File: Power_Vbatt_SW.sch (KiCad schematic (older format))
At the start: 14 parts, among them P5 XT60, Q1 IPD90P03P4L, Q2 BC817-40SMD, Q31 IPD90P03P4L

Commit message: Add more connector for thruster channels
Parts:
- added P2, P3, P4: XT60, Zeabus:XT60, symbol XT60
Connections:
- wire segments 30 -> 36
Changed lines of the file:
@@
 AR Path="/5625A3C6/56273268" Ref="Q18"  Part="1"
 AR Path="/5625A3D6/56273268" Ref="Q20"  Part="1"
-AR Path="/56273268" Ref="Q2"  Part="1"
-F 0 "Q2" H 5800 3775 50  0000 L CNN
+AR Path="/56273268" Ref="Q3"  Part="1"
+F 0 "Q3" H 5800 3775 50  0000 L CNN
 F 1 "BC817-40SMD" H 5800 3700 50  0000 L CNN
 F 2 "TO_SOT_Packages_SMD:SOT-23" H 5800 3625 50  0000 L CIN
@@
 AR Path="/5625A3C6/5627326B" Ref="#PWR048"  Part="1"
 AR Path="/5625A3D6/5627326B" Ref="#PWR051"  Part="1"
-AR Path="/5627326B" Ref="#PWR01"  Part="1"
-F 0 "#PWR01" H 5700 3700 50  0001 C CNN
+AR Path="/5627326B" Ref="#PWR1"  Part="1"
+F 0 "#PWR1" H 5700 3700 50  0001 C CNN
 F 1 "GND" H 5700 3800 50  0000 C CNN
 F 2 "" H 5700 3950 60  0000 C CNN
@@
 AR Path="/5625A3C6/5624F5C0" Ref="R45"  Part="1"
 AR Path="/5625A3D6/5624F5C0" Ref="R50"  Part="1"
-AR Path="/5624F5C0" Ref="R5"  Part="1"
-F 0 "R5" V 7380 4400 50  0000 C CNN
+AR Path="/5624F5C0" Ref="R6"  Part="1"
+F 0 "R6" V 7380 4400 50  0000 C CNN
 F 1 "1.2k" V 7300 4400 50  0000 C CNN
 F 2 "Resistors_SMD:R_0603" V 7230 4400 30  0001 C CNN
@@
 AR Path="/5625A3C6/5624F69A" Ref="R42"  Part="1"
 AR Path="/5625A3D6/5624F69A" Ref="R47"  Part="1"
-AR Path="/5624F69A" Ref="R2"  Part="1"
-F 0 "R2" V 6030 3350 50  0000 C CNN
+AR Path="/5624F69A" Ref="R3"  Part="1"
+F 0 "R3" V 6030 3350 50  0000 C CNN
 F 1 "100" V 5950 3350 50  0000 C CNN
 F 2 "Resistors_SMD:R_0603" V 5880 3350 30  0001 C CNN
@@
 AR Path="/5625A3C6/5624F6C3" Ref="R44"  Part="1"
 AR Path="/5625A3D6/5624F6C3" Ref="R49"  Part="1"
-AR Path="/5624F6C3" Ref="R4"  Part="1"
-F 0 "R4" V 5230 3700 50  0000 C CNN
+AR Path="/5624F6C3" Ref="R5"  Part="1"
+F 0 "R5" V 5230 3700 50  0000 C CNN
 F 1 "330" V 5150 3700 50  0000 C CNN
 F 2 "Resistors_SMD:R_0603" V 5080 3700 30  0001 C CNN
@@
 AR Path="/5625A3C6/5624F6F4" Ref="R43"  Part="1"
 AR Path="/5625A3D6/5624F6F4" Ref="R48"  Part="1"
-AR Path="/5624F6F4" Ref="R3"  Part="1"
-F 0 "R3" V 4530 3700 50  0000 C CNN
+AR Path="/5624F6F4" Ref="R4"  Part="1"
+F 0 "R4" V 4530 3700 50  0000 C CNN
 F 1 "2.2k" V 4450 3700 50  0000 C CNN
 F 2 "Resistors_SMD:R_0603" V 4380 3700 30  0001 C CNN
@@
 AR Path="/5625A3C6/56273271" Ref="#PWR049"  Part="1"
 AR Path="/5625A3D6/56273271" Ref="#PWR052"  Part="1"
-AR Path="/56273271" Ref="#PWR02"  Part="1"
-F 0 "#PWR02" H 7650 4650 50  0001 C CNN
+AR Path="/56273271" Ref="#PWR3"  Part="1"
+F 0 "#PWR3" H 7650 4650 50  0001 C CNN
 F 1 "GND" H 7650 4750 50  0000 C CNN
 F 2 "" H 7650 4900 60  0000 C CNN
@@
 AR Path="/5625A3C6/562508C1" Ref="#PWR050"  Part="1"
 AR Path="/5625A3D6/562508C1" Ref="#PWR053"  Part="1"
-AR Path="/562508C1" Ref="#PWR03"  Part="1"
-F 0 "#PWR03" H 4900 3850 50  0001 C CNN
+AR Path="/562508C1" Ref="#PWR2"  Part="1"
+F 0 "#PWR2" H 4900 3850 50  0001 C CNN
 F 1 "GND" H 4900 3950 50  0000 C CNN
 F 2 "" H 4900 4100 60  0000 C CNN
@@
 AR Path="/5625A3C6/5626EEE6" Ref="P13"  Part="1"
 AR Path="/5625A3D6/5626EEE6" Ref="P14"  Part="1"
-AR Path="/5626EEE6" Ref="P5"  Part="1"
-F 0 "P5" H 7850 4650 50  0000 C CNN
+AR Path="/5626EEE6" Ref="P1"  Part="1"
+F 0 "P1" H 7850 4650 50  0000 C CNN
 F 1 "XT60" H 7850 4350 50  0000 C CNN
 F 2 "Zeabus:XT60" H 7850 4500 60  0001 C CNN
@@
 	7650 4050 7650 4450
 Wire Wire Line
-	7300 4250 7650 4250
+	7300 4250 8850 4250
 Wire Wire Line
 	7300 4550 7300 4600
@@
 	7300 4800 7300 4900
 Wire Wire Line
-	7300 4900 7650 4900
+	7300 4900 8850 4900
 Connection ~ 7650 4900
 Wire Wire Line
@@
 AR Path="/5625A3C6/56621CAF" Ref="Q39"  Part="1"
 AR Path="/5625A3D6/56621CAF" Ref="Q40"  Part="1"
-AR Path="/56621CAF" Ref="Q31"  Part="1"
-F 0 "Q31" H 6900 2500 50  0000 R CNN
+AR Path="/56621CAF" Ref="Q1"  Part="1"
+F 0 "Q1" H 6900 2500 50  0000 R CNN
 F 1 "IPD90P03P4L" H 7250 2400 50  0000 R CNN
 F 2 "TO_SOT_Packages_SMD:TO-252-2Lead" H 6800 2550 29  0001 C CNN
@@
 AR Path="/5625A3C6/56621CBB" Ref="R77"  Part="1"
 AR Path="/5625A3D6/56621CBB" Ref="R79"  Part="1"
-AR Path="/56621CBB" Ref="R6"  Part="1"
-F 0 "R6" V 6030 2450 50  0000 C CNN
+AR Path="/56621CBB" Ref="R2"  Part="1"
+F 0 "R2" V 6030 2450 50  0000 C CNN
 F 1 "100" V 5950 2450 50  0000 C CNN
 F 2 "Resistors_SMD:R_0603" V 5880 2450 30  0001 C CNN
@@
 AR Path="/5625A3C6/5627326A" Ref="Q17"  Part="1"
 AR Path="/5625A3D6/5627326A" Ref="Q19"  Part="1"
-AR Path="/5627326A" Ref="Q1"  Part="1"
-F 0 "Q1" H 6900 3400 50  0000 R CNN
+AR Path="/5627326A" Ref="Q2"  Part="1"
+F 0 "Q2" H 6900 3400 50  0000 R CNN
 F 1 "IPD90P03P4L" H 7250 3300 50  0000 R CNN
 F 2 "TO_SOT_Packages_SMD:TO-252-2Lead" H 6800 3450 29  0001 C CNN
@@
 Text HLabel 7700 2200 2    60   Output ~ 0
 SW_Switch_C
+$Comp
+L XT60 P2
+U 1 1 58CA94E8
+P 8250 4500
+F 0 "P2" H 8250 4650 50  0000 C CNN
+F 1 "XT60" H 8250 4350 50  0000 C CNN
+F 2 "Zeabus:XT60" H 8250 4500 60  0001 C CNN
+F 3 "" H 8250 4500 60  0000 C CNN
+	1    8250 4500
+	1    0    0    -1
+$EndComp
+$Comp
+L XT60 P3
+U 1 1 58CA9529
+P 8650 4500
+F 0 "P3" H 8650 4650 50  0000 C CNN
+F 1 "XT60" H 8650 4350 50  0000 C CNN
+F 2 "Zeabus:XT60" H 8650 4500 60  0001 C CNN
+F 3 "" H 8650 4500 60  0000 C CNN
+	1    8650 4500
+	1    0    0    -1
+$EndComp
+$Comp
+L XT60 P4
+U 1 1 58CA956E
+P 9050 4500
+F 0 "P4" H 9050 4650 50  0000 C CNN
+F 1 "XT60" H 9050 4350 50  0000 C CNN
+F 2 "Zeabus:XT60" H 9050 4500 60  0001 C CNN
+F 3 "" H 9050 4500 60  0000 C CNN
+	1    9050 4500
+	1    0    0    -1
+$EndComp
+Wire Wire Line
+	8850 4250 8850 4450
+Wire Wire Line
+	8850 4900 8850 4550
+Wire Wire Line
+	8050 4450 8050 4250
+Connection ~ 8050 4250
+Wire Wire Line
+	8450 4450 8450 4250
+Connection ~ 8450 4250
+Wire Wire Line
+	8450 4550 8450 4900
+Connection ~ 8450 4900
+Wire Wire Line
+	8050 4550 8050 4900
+Connection ~ 8050 4900
 $EndSCHEMATC

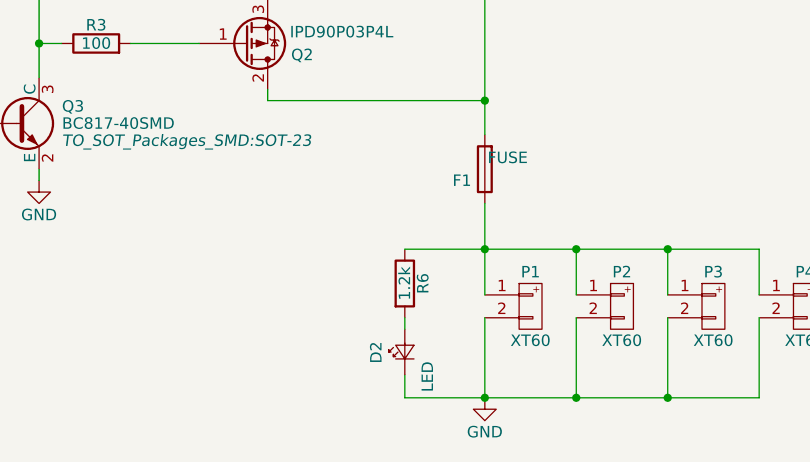
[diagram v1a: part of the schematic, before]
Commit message: Change the resistor value of the LED from 1.2k to 2.2k because the battery voltage is double from the previous version
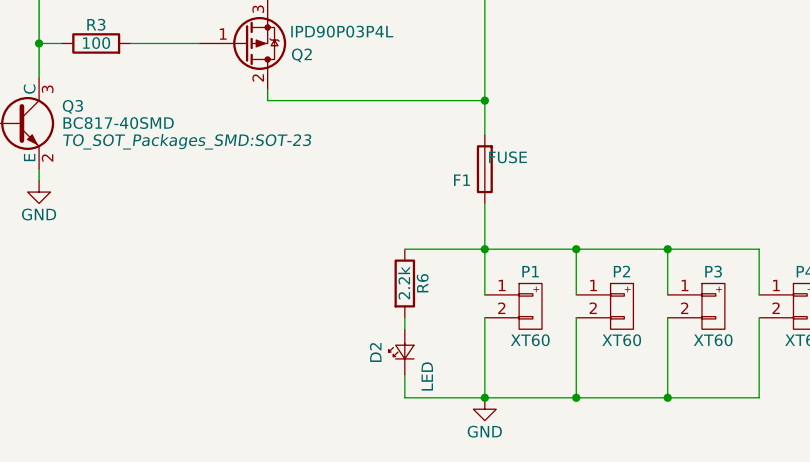
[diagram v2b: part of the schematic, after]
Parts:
- R5: value 1.2k -> 2.2k
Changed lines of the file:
@@
 AR Path="/5625A3C6/5627326B" Ref="#PWR048"  Part="1"
 AR Path="/5625A3D6/5627326B" Ref="#PWR051"  Part="1"
-AR Path="/5627326B" Ref="#PWR1"  Part="1"
-F 0 "#PWR1" H 5700 3700 50  0001 C CNN
+AR Path="/5627326B" Ref="#PWR01"  Part="1"
+F 0 "#PWR01" H 5700 3700 50  0001 C CNN
 F 1 "GND" H 5700 3800 50  0000 C CNN
 F 2 "" H 5700 3950 60  0000 C CNN
@@
 AR Path="/5624F5C0" Ref="R6"  Part="1"
 F 0 "R6" V 7380 4400 50  0000 C CNN
-F 1 "1.2k" V 7300 4400 50  0000 C CNN
+F 1 "2.2k" V 7300 4400 50  0000 C CNN
 F 2 "Resistors_SMD:R_0603" V 7230 4400 30  0001 C CNN
 F 3 "" H 7300 4400 30  0000 C CNN
@@
 AR Path="/5625A3C6/56273271" Ref="#PWR049"  Part="1"
 AR Path="/5625A3D6/56273271" Ref="#PWR052"  Part="1"
-AR Path="/56273271" Ref="#PWR3"  Part="1"
-F 0 "#PWR3" H 7650 4650 50  0001 C CNN
+AR Path="/56273271" Ref="#PWR02"  Part="1"
+F 0 "#PWR02" H 7650 4650 50  0001 C CNN
 F 1 "GND" H 7650 4750 50  0000 C CNN
 F 2 "" H 7650 4900 60  0000 C CNN
@@
 AR Path="/5625A3C6/562508C1" Ref="#PWR050"  Part="1"
 AR Path="/5625A3D6/562508C1" Ref="#PWR053"  Part="1"
-AR Path="/562508C1" Ref="#PWR2"  Part="1"
-F 0 "#PWR2" H 4900 3850 50  0001 C CNN
+AR Path="/562508C1" Ref="#PWR03"  Part="1"
+F 0 "#PWR03" H 4900 3850 50  0001 C CNN
 F 1 "GND" H 4900 3950 50  0000 C CNN
 F 2 "" H 4900 4100 60  0000 C CNN
